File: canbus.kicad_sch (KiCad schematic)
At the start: 19 parts, among them J501 Conn_01x02, J601 Conn_01x04, U501 SN65HVD231, U502 ADuM1201AR, U603 PJ75AL33SA

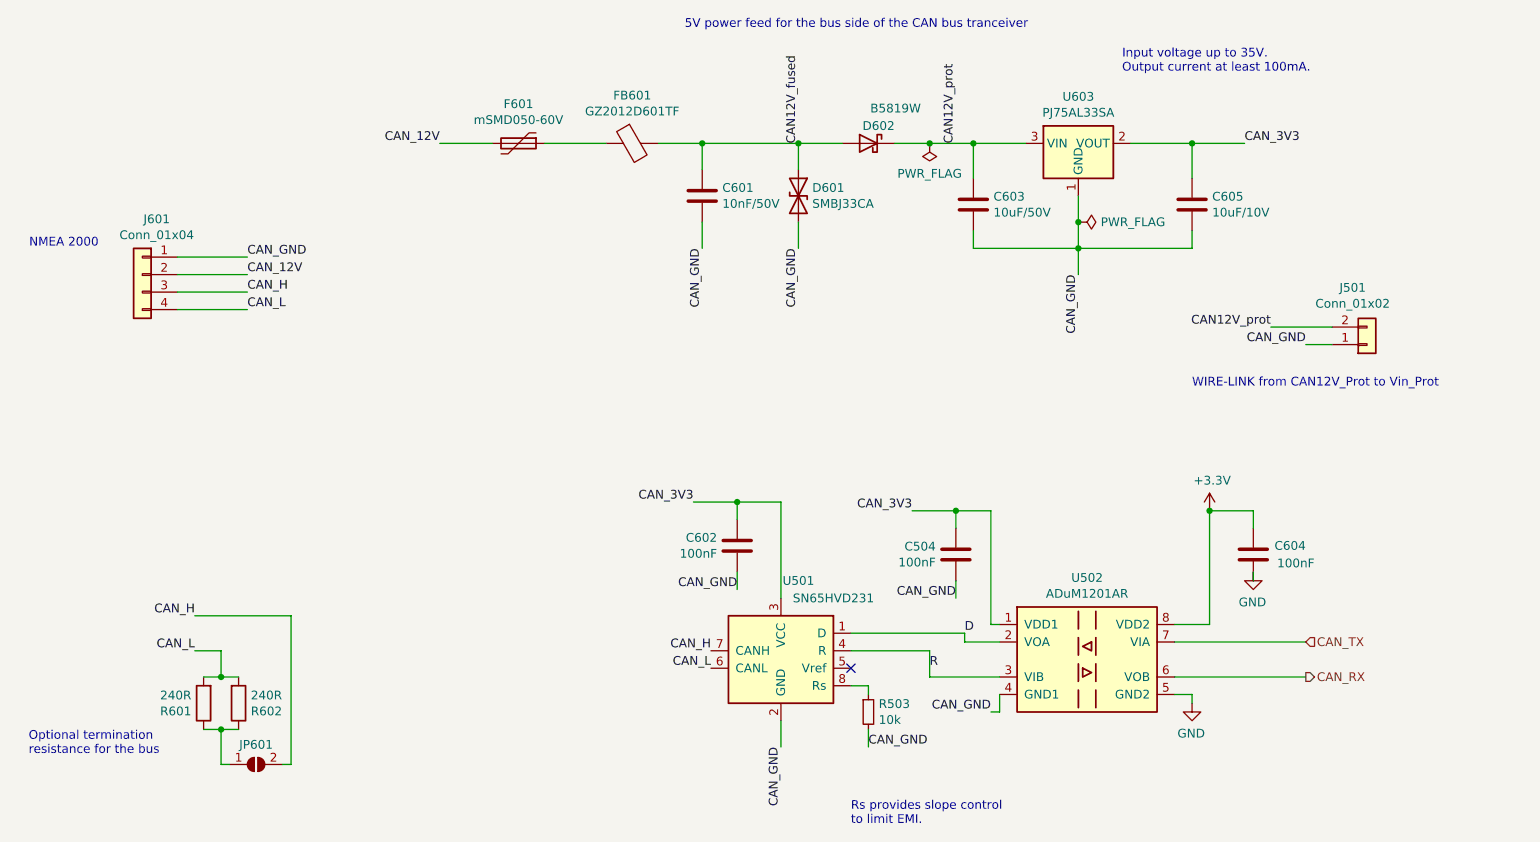
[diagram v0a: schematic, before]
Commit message: Bump version to 2.0.1, update the components for availability
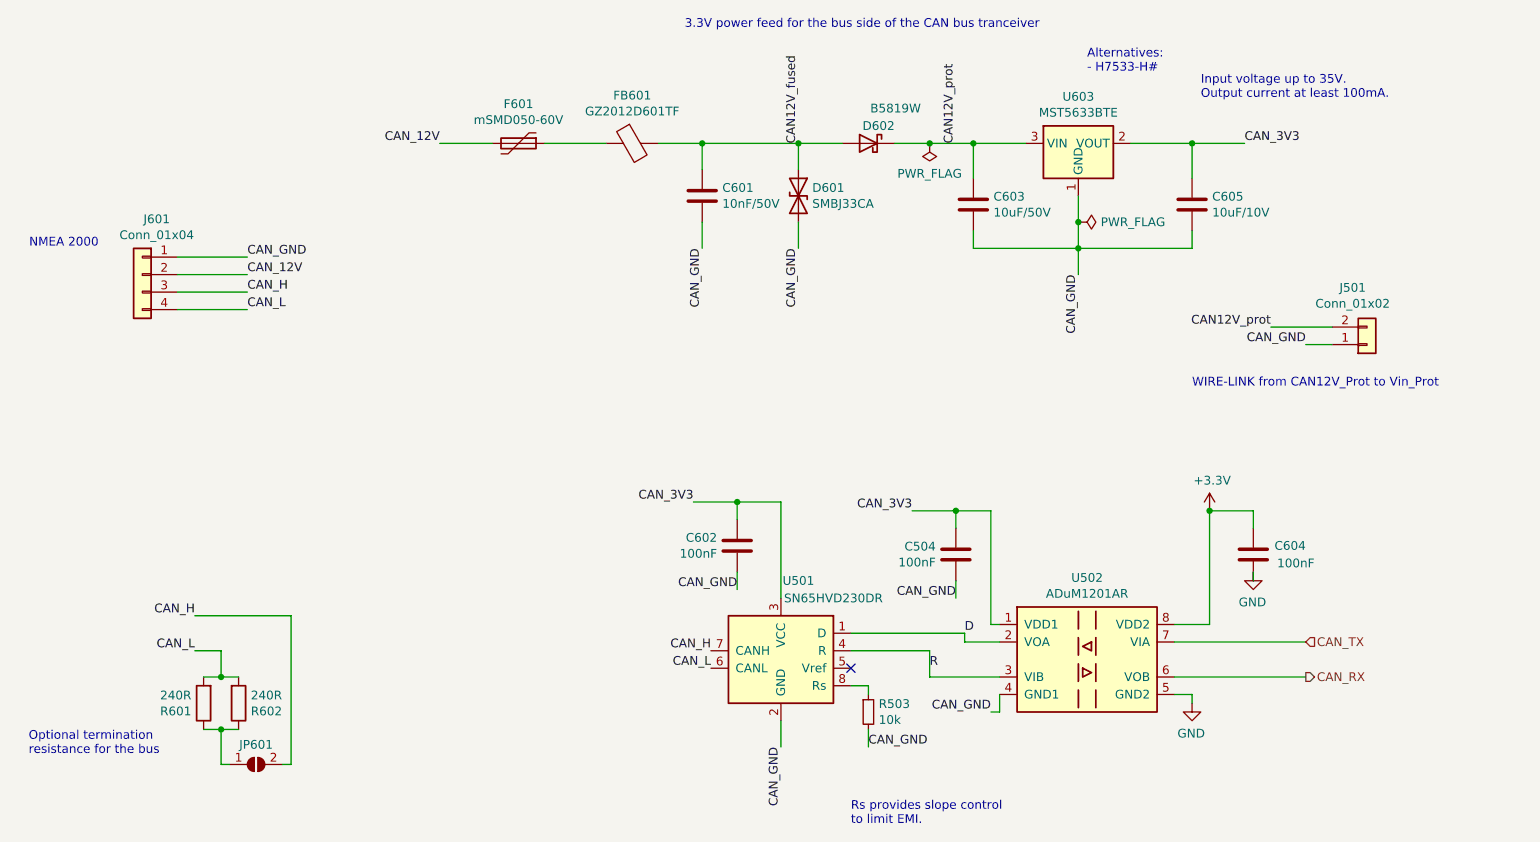
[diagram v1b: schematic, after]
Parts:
- U501: value SN65HVD231 -> SN65HVD230DR; LCSC C129257 -> C12084
- U603: value PJ75AL33SA -> MST5633BTE; LCSC C411736 -> C525415
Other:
- note added: "3.3V power feed for the bus side of the CAN bus tranceiver"
- note added: "Alternatives: - H7533-H#"
- note removed: "5V power feed for the bus side of the CAN bus tranceiver"
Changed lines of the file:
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@@
   (title_block
     (title "Sailor Hat with ESP32")
-    (date "2021-08-17")
-    (rev "2.0.0")
+    (date "2021-12-31")
+    (rev "2.0.1")
     (company "Hat Labs Ltd")
     (comment 1 "https://creativecommons.org/licenses/by-sa/4.0")
@@
     (stroke (width 0) (type default) (color 0 0 0 0))
   )
-  (text "5V power feed for the bus side of the CAN bus tranceiver"
+  (text "3.3V power feed for the bus side of the CAN bus tranceiver"
     (at 120.65 20.32 0)
     (effects (font (size 1.27 1.27)) (justify left bottom))
@@
   )
   (text "Input voltage up to 35V.\nOutput current at least 100mA."
-    (at 184.15 26.67 0)
+    (at 195.58 30.48 0)
     (effects (font (size 1.27 1.27)) (justify left bottom))
   )
   (text "Optional termination\nresistance for the bus" (at 25.4 125.73 0)
+    (effects (font (size 1.27 1.27)) (justify left bottom))
+  )
+  (text "Alternatives:\n- H7533-H#" (at 179.07 26.67 0)
     (effects (font (size 1.27 1.27)) (justify left bottom))
   )
@@
     (pin "1")
   )
-  (symbol (lib_id "Device:C") (at 203.2 96.52 0) (mirror y)
+  (symbol (lib_id "Device:C") (at 203.2 96.52 0) (mirror y) (unit 1)
     (in_bom yes) (on_board yes)
     (property "Reference" "C604" (id 0) (at 210.82 95.25 0)
@@
     (pin "1")
   )
-  (symbol (lib_id "Device:C") (at 128.27 95.25 0) (mirror y)
+  (symbol (lib_id "Device:C") (at 128.27 95.25 0) (mirror y) (unit 1)
     (in_bom yes) (on_board yes)
     (property "Reference" "C602" (id 0) (at 125.349 94.0816 0)
@@
     (pin "1")
   )
-  (symbol (lib_id "SH-ESP32:HT75xx-1-SOT23") (at 177.8 39.37 0)
+  (symbol (lib_id "SH-ESP32:HT75xx-1-SOT23") (at 177.8 39.37 0) (unit 1)
     (in_bom yes) (on_board yes)
     (property "Reference" "U603" (id 0) (at 177.8 30.0482 0))
-    (property "Value" "PJ75AL33SA" (id 1) (at 177.8 32.3596 0))
+    (property "Value" "MST5633BTE" (id 1) (at 177.8 32.3596 0))
     (property "Footprint" "Package_TO_SOT_SMD:SOT-23" (id 2) (at 177.8 31.115 0)
       (effects (font (size 1.27 1.27) italic) hide)
     )
-    (property "Datasheet" "" (id 3) (at 177.8 36.83 0)
-      (effects (font (size 1.27 1.27)) hide)
-    )
-    (property "LCSC" "C411736" (id 4) (at 177.8 39.37 0)
+    (property "Datasheet" "https://datasheet.lcsc.com/lcsc/2005041732_MST-MST5633BTE_C525415.pdf" (id 3) (at 177.8 36.83 0)
+      (effects (font (size 1.27 1.27)) hide)
+    )
+    (property "LCSC" "C525415" (id 4) (at 177.8 39.37 0)
       (effects (font (size 1.27 1.27)) hide)
     )
@@
     (pin "3")
   )
-  (symbol (lib_id "Device:Polyfuse") (at 96.52 36.83 270)
+  (symbol (lib_id "Device:Polyfuse") (at 96.52 36.83 270) (unit 1)
     (in_bom yes) (on_board yes)
     (property "Reference" "F601" (id 0) (at 96.52 31.115 90))
@@
     (pin "2")
   )
-  (symbol (lib_id "Device:D_TVS") (at 137.16 44.45 270)
+  (symbol (lib_id "Device:D_TVS") (at 137.16 44.45 270) (unit 1)
     (in_bom yes) (on_board yes)
     (property "Reference" "D601" (id 0) (at 139.1666 43.2816 90)
@@
     (pin "2")
   )
-  (symbol (lib_id "power:PWR_FLAG") (at 156.21 36.83 180)
+  (symbol (lib_id "power:PWR_FLAG") (at 156.21 36.83 180) (unit 1)
     (in_bom yes) (on_board yes)
     (property "Reference" "#FLG0601" (id 0) (at 156.21 38.735 0)
@@
     (pin "1")
   )
-  (symbol (lib_id "power:PWR_FLAG") (at 177.8 48.26 270)
+  (symbol (lib_id "power:PWR_FLAG") (at 177.8 48.26 270) (unit 1)
     (in_bom yes) (on_board yes)
     (property "Reference" "#FLG0602" (id 0) (at 179.705 48.26 0)
@@
     (pin "1")
   )
-  (symbol (lib_id "Device:C") (at 162.56 45.72 0)
+  (symbol (lib_id "Device:C") (at 162.56 45.72 0) (unit 1)
     (in_bom yes) (on_board yes)
     (property "Reference" "C603" (id 0) (at 165.481 44.5516 0)
@@
     (pin "2")
   )
-  (symbol (lib_id "Device:C") (at 194.31 45.72 0)
+  (symbol (lib_id "Device:C") (at 194.31 45.72 0) (unit 1)
     (in_bom yes) (on_board yes)
     (property "Reference" "C605" (id 0) (at 197.231 44.5516 0)
@@
     (pin "2")
   )
-  (symbol (lib_id "Device:Ferrite_Bead") (at 113.03 36.83 90) (mirror x)
+  (symbol (lib_id "Device:Ferrite_Bead") (at 113.03 36.83 90) (mirror x) (unit 1)
     (in_bom yes) (on_board yes)
     (property "Reference" "FB601" (id 0) (at 113.03 29.8704 90))
@@
     (pin "4")
   )
-  (symbol (lib_id "Device:D_Schottky") (at 147.32 36.83 0) (mirror y)
+  (symbol (lib_id "Device:D_Schottky") (at 147.32 36.83 0) (mirror y) (unit 1)
     (in_bom yes) (on_board yes)
     (property "Reference" "D602" (id 0) (at 151.13 34.29 0)
@@
     (pin "2")
   )
-  (symbol (lib_id "Device:C") (at 123.19 44.45 0)
+  (symbol (lib_id "Device:C") (at 123.19 44.45 0) (unit 1)
     (in_bom yes) (on_board yes)
     (property "Reference" "C601" (id 0) (at 126.111 43.2816 0)
@@
     (pin "8")
   )
-  (symbol (lib_id "Device:C") (at 160.02 96.52 0) (mirror y)
+  (symbol (lib_id "Device:C") (at 160.02 96.52 0) (mirror y) (unit 1)
     (in_bom yes) (on_board yes)
     (property "Reference" "C504" (id 0) (at 157.099 95.3516 0)
@@
     (in_bom yes) (on_board yes)
     (property "Reference" "U501" (id 0) (at 137.16 100.33 0))
-    (property "Value" "SN65HVD231" (id 1) (at 142.24 102.87 0))
+    (property "Value" "SN65HVD230DR" (id 1) (at 142.24 102.87 0))
     (property "Footprint" "Package_SO:SOIC-8_3.9x4.9mm_P1.27mm" (id 2) (at 134.62 123.19 0)
       (effects (font (size 1.27 1.27)) hide)
@@
       (effects (font (size 1.27 1.27)) hide)
     )
-    (property "LCSC" " C129257" (id 4) (at 134.62 110.49 0)
+    (property "LCSC" "C12084" (id 4) (at 134.62 110.49 0)
       (effects (font (size 1.27 1.27)) hide)
     )
@@
     (pin "2")
   )
-  (symbol (lib_id "Connector_Generic:Conn_01x02") (at 219.71 66.04 0) (mirror x)
+  (symbol (lib_id "Connector_Generic:Conn_01x02") (at 219.71 66.04 0) (mirror x) (unit 1)
     (in_bom yes) (on_board yes)
     (property "Reference" "J501" (id 0) (at 217.6272 57.785 0))

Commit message: Rename Ferrite_Bead to FerriteBead
Symbol name changed between KiCad 5 and 6...
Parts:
- FB601: symbol Device:Ferrite_Bead -> Device:FerriteBead
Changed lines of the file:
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@@
     (pin "2")
   )
-  (symbol (lib_id "Device:Ferrite_Bead") (at 113.03 36.83 90) (mirror x) (unit 1)
+  (symbol (lib_id "Device:FerriteBead") (at 113.03 36.83 90) (mirror x) (unit 1)
     (in_bom yes) (on_board yes)
     (property "Reference" "FB601" (id 0) (at 113.03 29.8704 90))

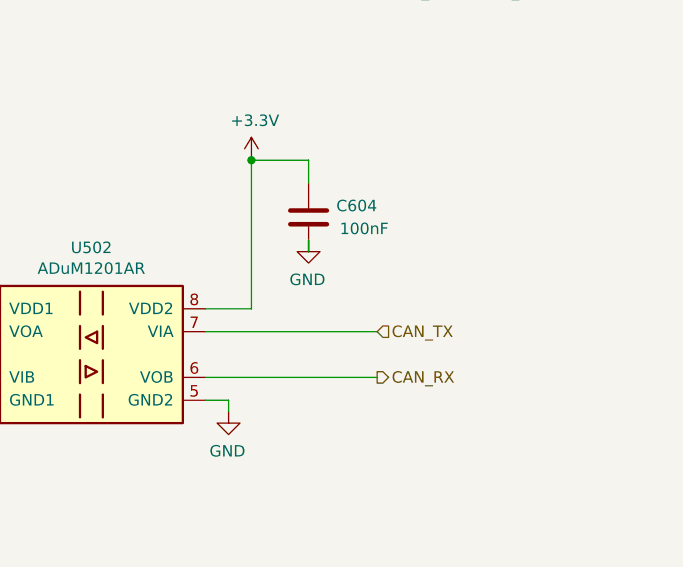
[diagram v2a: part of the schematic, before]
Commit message: Add a pull-up resistor to CAN TX line
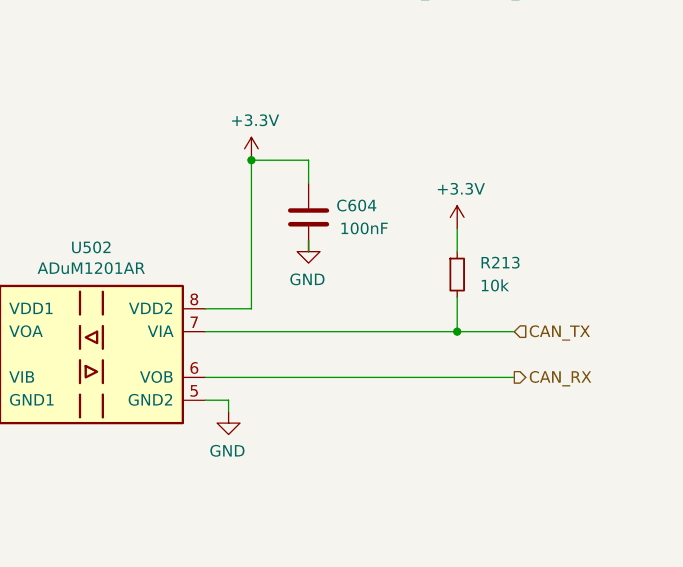
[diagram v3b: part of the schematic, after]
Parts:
- added R213: 10k, Resistor_SMD:R_0402_1005Metric, symbol Device:R_Small
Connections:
- net +3V3: now also R213.1
- net CAN_TX: now also R213.2
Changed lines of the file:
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@@
   (junction (at 137.16 36.83) (diameter 0) (color 0 0 0 0)
+  )
+  (junction (at 219.71 109.22) (diameter 0) (color 0 0 0 0)
   )
   (junction (at 128.27 88.9) (diameter 0) (color 0 0 0 0)
@@
     (stroke (width 0) (type default) (color 0 0 0 0))
   )
+  (wire (pts (xy 219.71 109.22) (xy 226.06 109.22))
+    (stroke (width 0) (type default) (color 0 0 0 0))
+  )
   (wire (pts (xy 53.34 121.92) (xy 55.88 121.92))
     (stroke (width 0) (type default) (color 0 0 0 0))
@@
     (stroke (width 0) (type default) (color 0 0 0 0))
   )
+  (wire (pts (xy 219.71 105.41) (xy 219.71 109.22))
+    (stroke (width 0) (type default) (color 0 0 0 0))
+  )
   (wire (pts (xy 62.23 127) (xy 63.5 127))
     (stroke (width 0) (type default) (color 0 0 0 0))
@@
     (stroke (width 0) (type default) (color 0 0 0 0))
   )
+  (wire (pts (xy 191.77 114.3) (xy 226.06 114.3))
+    (stroke (width 0) (type default) (color 0 0 0 0))
+  )
   (wire (pts (xy 161.29 109.22) (xy 161.29 107.95))
     (stroke (width 0) (type default) (color 0 0 0 0))
@@
     (stroke (width 0) (type default) (color 0 0 0 0))
   )
+  (wire (pts (xy 191.77 109.22) (xy 219.71 109.22))
+    (stroke (width 0) (type default) (color 0 0 0 0))
+  )
   (wire (pts (xy 214.63 66.04) (xy 210.82 66.04))
     (stroke (width 0) (type default) (color 0 0 0 0))
   )
-  (wire (pts (xy 191.77 109.22) (xy 210.82 109.22))
-    (stroke (width 0) (type default) (color 0 0 0 0))
-  )
   (wire (pts (xy 49.53 110.49) (xy 53.34 110.49))
     (stroke (width 0) (type default) (color 0 0 0 0))
@@
     (stroke (width 0) (type default) (color 0 0 0 0))
   )
-  (wire (pts (xy 191.77 114.3) (xy 210.82 114.3))
+  (wire (pts (xy 219.71 97.79) (xy 219.71 100.33))
     (stroke (width 0) (type default) (color 0 0 0 0))
   )
@@
     (effects (font (size 1.27 1.27)) (justify left bottom))
   )
-  (hierarchical_label "CAN_TX" (shape input) (at 210.82 109.22 0)
+  (hierarchical_label "CAN_TX" (shape input) (at 226.06 109.22 0)
     (effects (font (size 1.27 1.27)) (justify left))
   )
-  (hierarchical_label "CAN_RX" (shape output) (at 210.82 114.3 0)
+  (hierarchical_label "CAN_RX" (shape output) (at 226.06 114.3 0)
     (effects (font (size 1.27 1.27)) (justify left))
   )
@@
     (pin "2")
   )
+  (symbol (lib_id "Device:R_Small") (at 219.71 102.87 0) (unit 1)
+    (in_bom yes) (on_board yes) (fields_autoplaced)
+    (property "Reference" "R213" (id 0) (at 222.25 101.5999 0)
+      (effects (font (size 1.27 1.27)) (justify left))
+    )
+    (property "Value" "10k" (id 1) (at 222.25 104.1399 0)
+      (effects (font (size 1.27 1.27)) (justify left))
+    )
+    (property "Footprint" "Resistor_SMD:R_0402_1005Metric" (id 2) (at 219.71 102.87 0)
+      (effects (font (size 1.27 1.27)) hide)
+    )
+    (property "Datasheet" "~" (id 3) (at 219.71 102.87 0)
+      (effects (font (size 1.27 1.27)) hide)
+    )
+    (property "LCSC" "C25744" (id 4) (at 219.71 102.87 0)
+      (effects (font (size 1.27 1.27)) hide)
+    )
+    (pin "1")
+    (pin "2")
+  )
+  (symbol (lib_id "power:+3.3V") (at 219.71 97.79 0) (unit 1)
+    (in_bom yes) (on_board yes)
+    (property "Reference" "#PWR0212" (id 0) (at 219.71 101.6 0)
+      (effects (font (size 1.27 1.27)) hide)
+    )
+    (property "Value" "+3.3V" (id 1) (at 220.091 93.3958 0))
+    (property "Footprint" "" (id 2) (at 219.71 97.79 0)
+      (effects (font (size 1.27 1.27)) hide)
+    )
+    (property "Datasheet" "" (id 3) (at 219.71 97.79 0)
+      (effects (font (size 1.27 1.27)) hide)
+    )
+    (pin "1")
+  )
 )
